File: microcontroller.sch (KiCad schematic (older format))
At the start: 61 parts, among them SW0 SW_Push, SW1 SW_Push, SW2 SW_Push, SW3 SW_Push, SW4 SW_Push, SW5 SW_Push

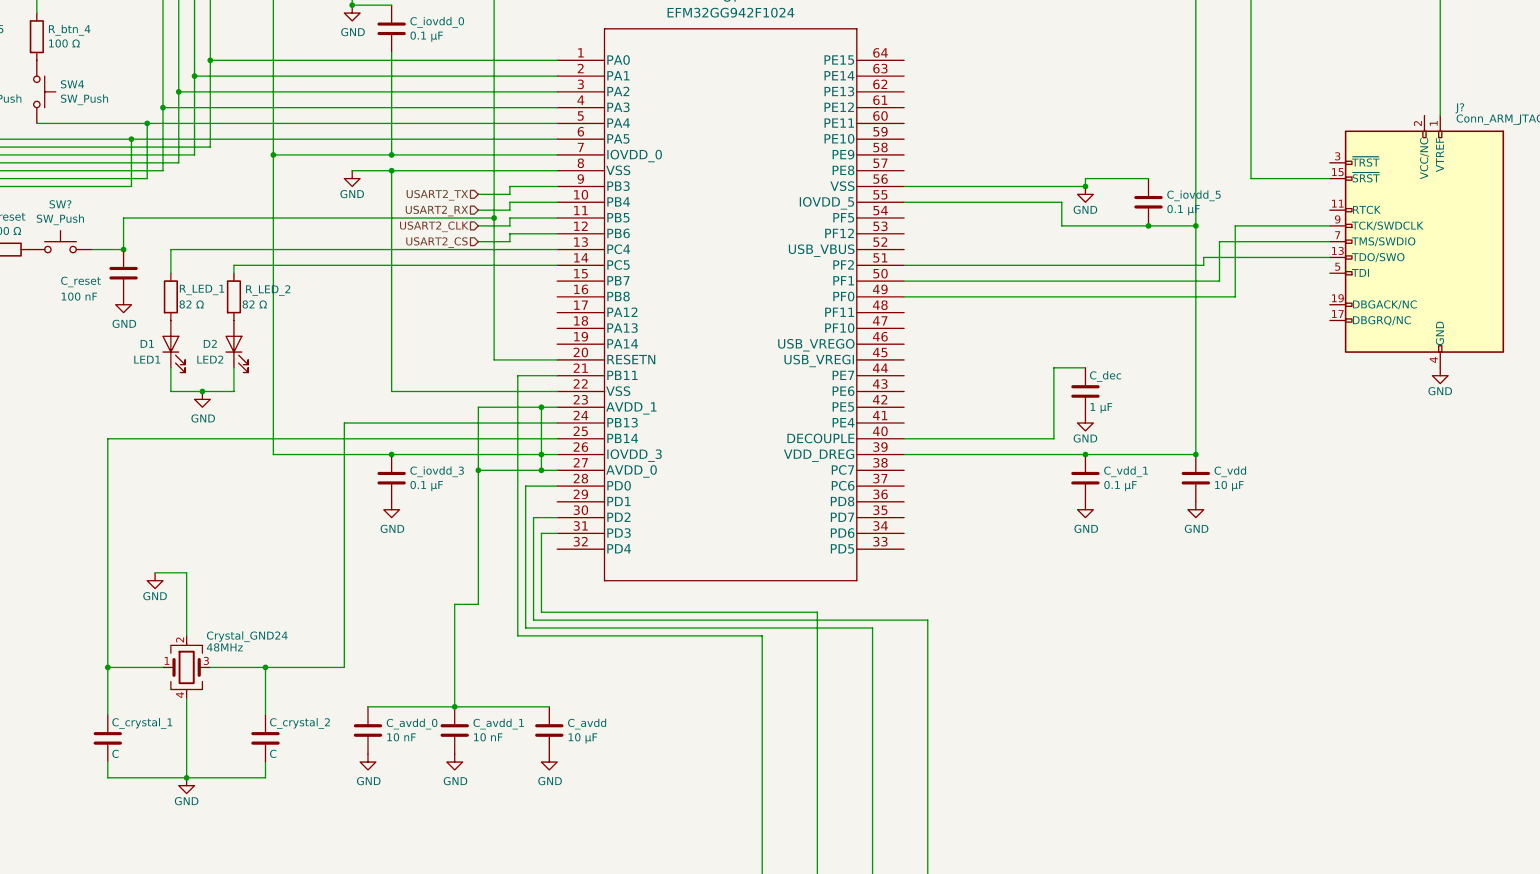
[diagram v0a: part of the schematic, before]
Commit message: Add NC symbols
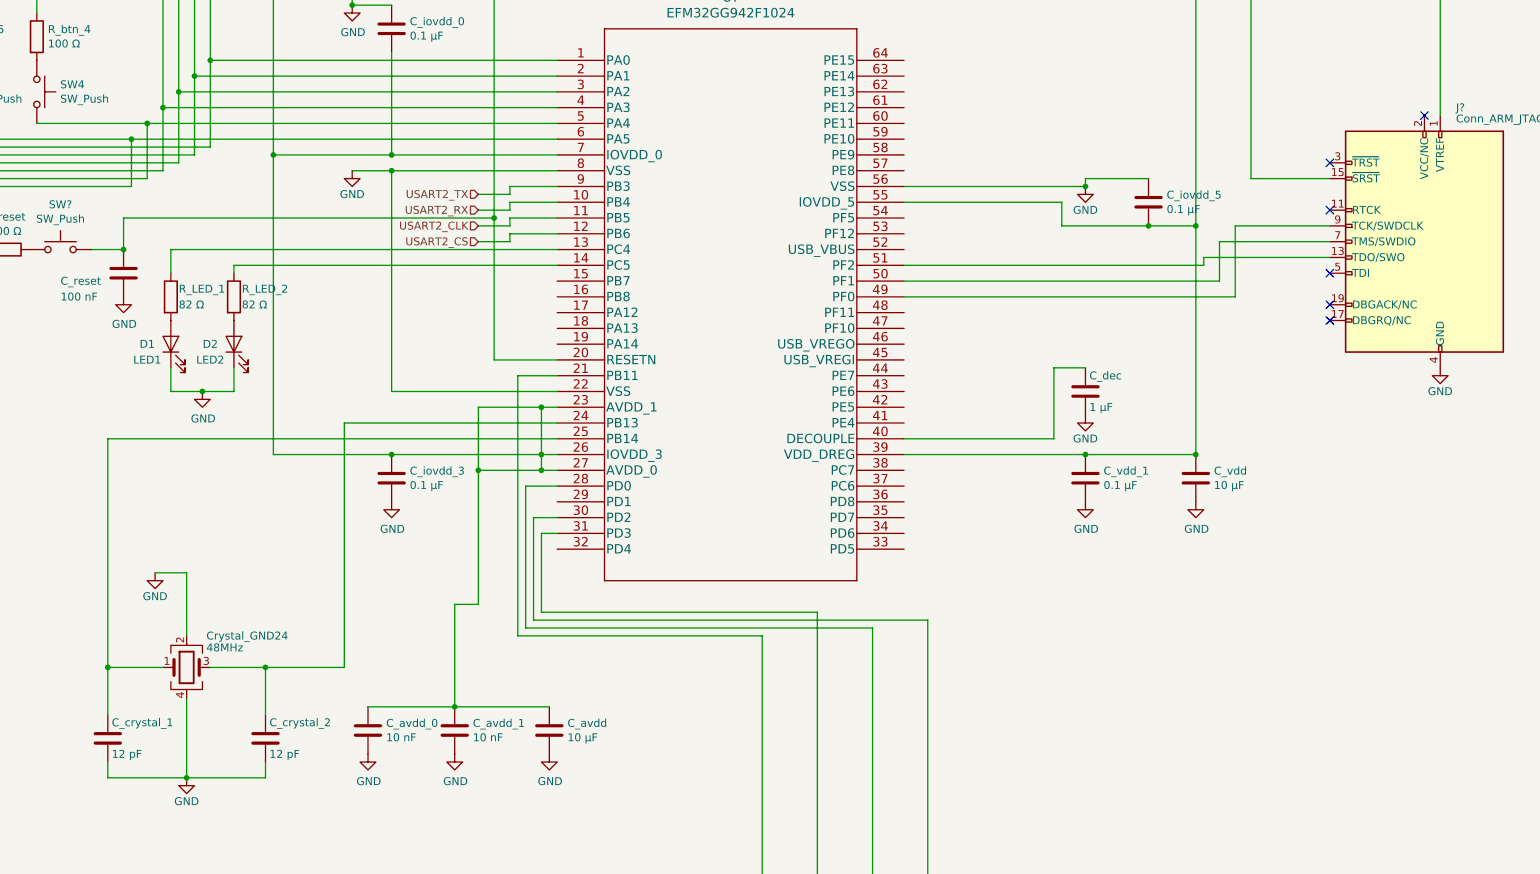
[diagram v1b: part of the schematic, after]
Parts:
- C_crystal_1, C_crystal_2: value C -> 12 pF
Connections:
- no-connect marks 2 -> 8
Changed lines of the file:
@@
 P 2600 6550
 F 0 "C_crystal_2" H 2625 6650 50  0000 L CNN
-F 1 "C" H 2625 6450 50  0000 L CNN
+F 1 "12 pF" H 2625 6450 50  0000 L CNN
 F 2 "" H 2638 6400 50  0001 C CNN
 F 3 "" H 2600 6550 50  0001 C CNN
@@
 P 1600 6550
 F 0 "C_crystal_1" H 1625 6650 50  0000 L CNN
-F 1 "C" H 1625 6450 50  0000 L CNN
+F 1 "12 pF" H 1625 6450 50  0000 L CNN
 F 2 "" H 1638 6400 50  0001 C CNN
 F 3 "" H 1600 6550 50  0001 C CNN
@@
 U 1 1 5D957EC3
 P 2400 3750
-F 0 "R_LED_2" H 2470 3796 50  0000 L CNN
+F 0 "R_LED_2" H 2450 3800 50  0000 L CNN
 F 1 "82 Ω" H 2450 3700 50  0000 L CNN
 F 2 "" V 2330 3750 50  0001 C CNN
@@
 Wire Wire Line
 	-1850 1200 -1550 1200
+NoConn ~ 9350 3200
+NoConn ~ 9350 2900
+NoConn ~ 9350 3800
+NoConn ~ 9350 3900
+NoConn ~ 9350 3600
+NoConn ~ 9950 2600
 $EndSCHEMATC

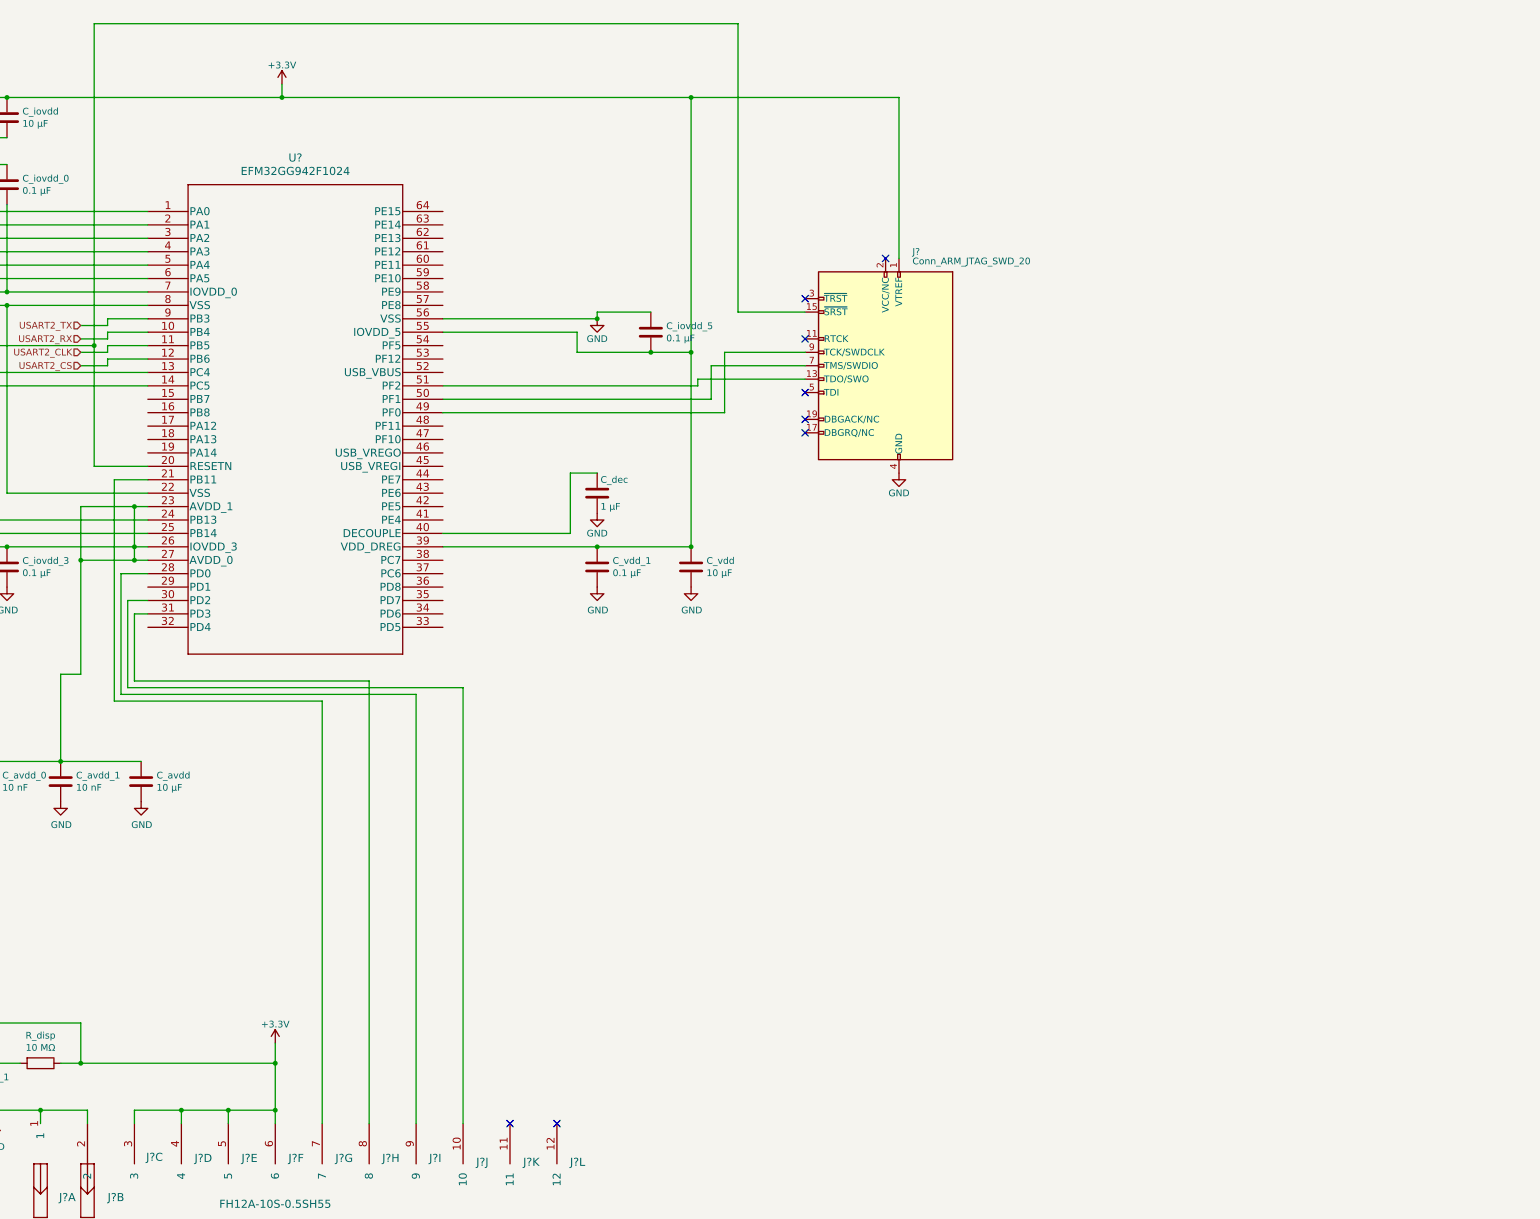
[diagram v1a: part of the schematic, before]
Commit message: Add 2x13 pin header
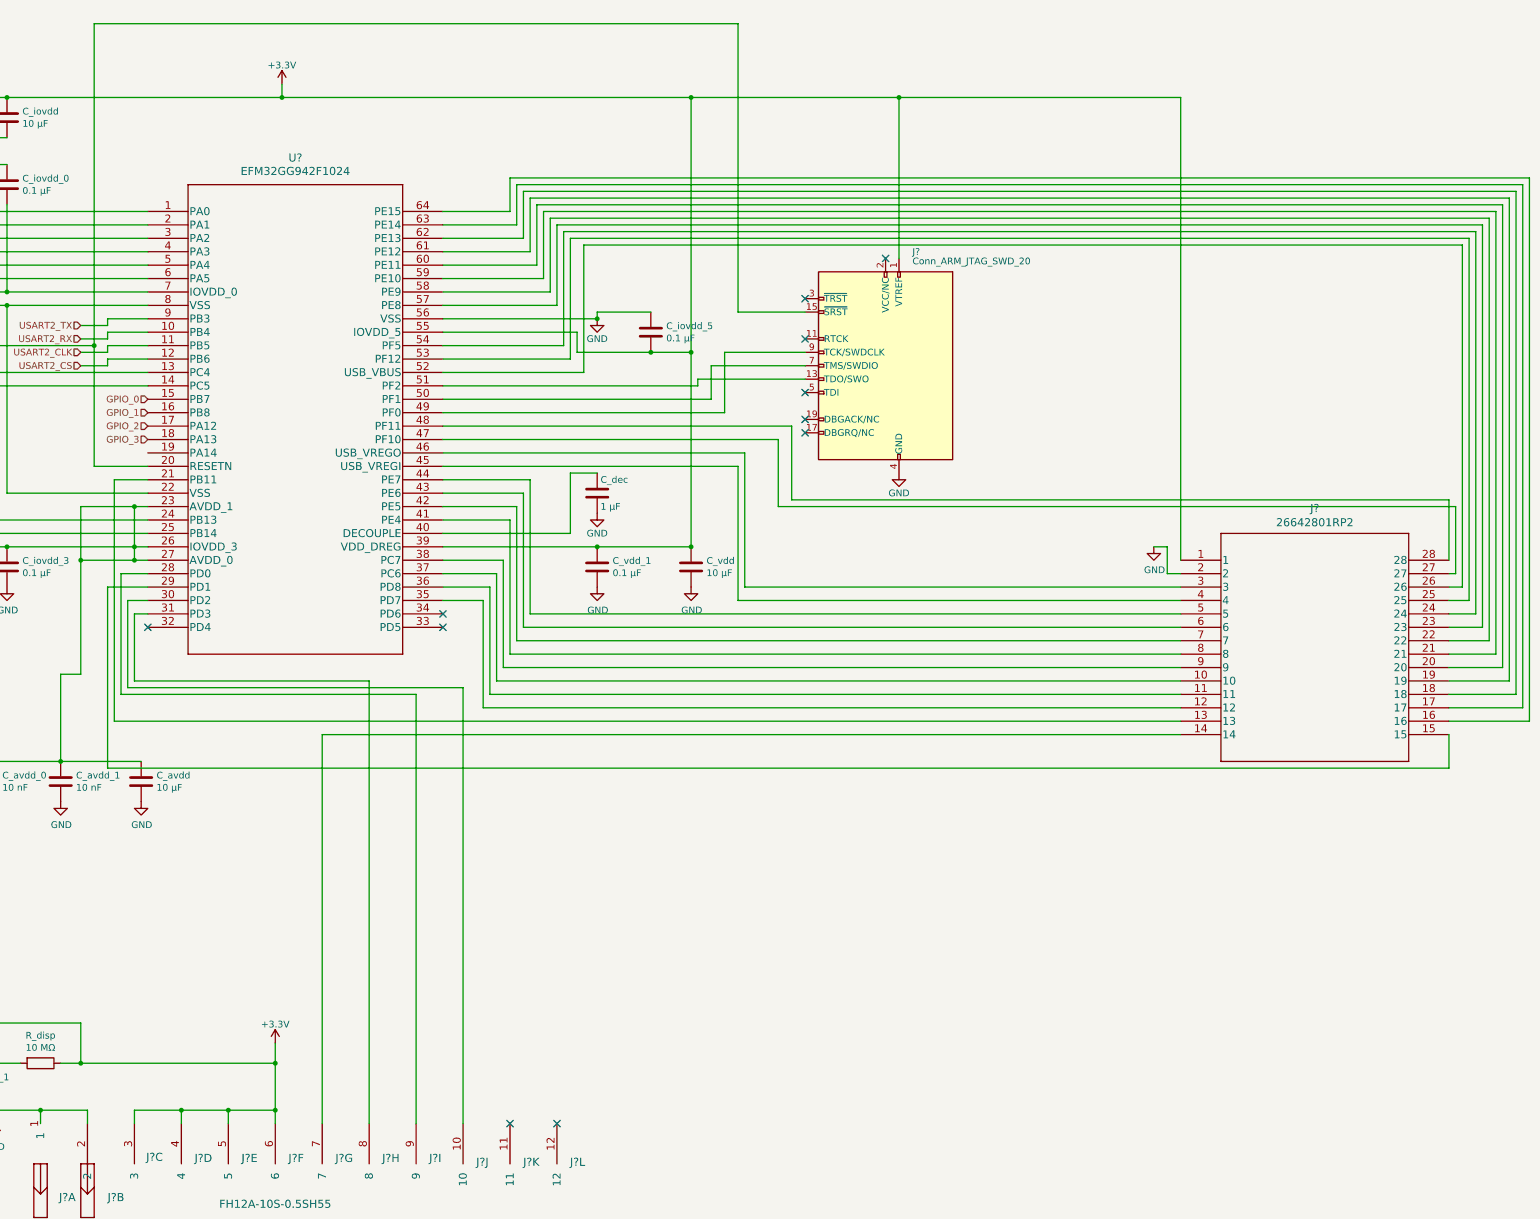
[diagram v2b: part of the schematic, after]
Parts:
- added J?: 26642801RP2, CON28_2X14_HDR_2664, symbol pin_header:26642801RP2
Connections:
- net +3V3: now also J?.1
- net GND: now also J?.2
- net GPIO_0: now reaches U?.15 (PB7)
- net GPIO_1: now reaches U?.16 (PB8)
- net GPIO_2: now reaches U?.17 (PA12)
- net GPIO_3: now reaches U?.18 (PA13)
- net at U?.21 (PB11): now also J?.13; no longer J?.7
- net at U?.29 (PD1): now also J?.15
- net at U?.35 (PD7): now also J?.12
- net at U?.36 (PD8): now also J?.11
- net at U?.37 (PC6): now also J?.10
- net at U?.38 (PC7): now also J?.9
- net at U?.41 (PE4): now also J?.8
- net at U?.42 (PE5): now also J?.7
- net at U?.43 (PE6): now also J?.6
- net at U?.44 (PE7): now also J?.5
- net at U?.45 (USB_VREGI): now also J?.4
- net at U?.46 (USB_VREGO): now also J?.3
- net at U?.47 (PF10): now also J?.27
- net at U?.48 (PF11): now also J?.28
- net at U?.52 (USB_VBUS): now also J?.26
- net at U?.53 (PF12): now also J?.25
- net at U?.54 (PF5): now also J?.24
- net at U?.57 (PE8): now also J?.23
- net at U?.58 (PE9): now also J?.22
- net at U?.59 (PE10): now also J?.21
- net at U?.60 (PE11): now also J?.20
- net at U?.61 (PE12): now also J?.19
- net at U?.62 (PE13): now also J?.18
- net at U?.63 (PE14): now also J?.17
- net at U?.64 (PE15): now also J?.16
- new net: J?.14, J?.7
- no-connect marks 8 -> 11
